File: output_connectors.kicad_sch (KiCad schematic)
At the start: 0 parts

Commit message: feat: add connector footprint and update PCB layout and schematic files
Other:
- added sheet 12V_pwm_fan_output_connector (12V_pwm_fan_output_connector.kicad_sch)
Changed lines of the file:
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@@
 	(generator_version "10.0")
 	(paper "A4")
+	(sheet
+		(at 40.64 36.83)
+		(size 26.67 17.78)
+		(exclude_from_sim no)
+		(in_bom yes)
+		(on_board yes)
+		(dnp no)
+		(fields_autoplaced yes)
+		(stroke
+			(width 0.1524)
+			(type solid)
+		)
+		(fill
+			(color 0 0 0 0)
+		)
+		(property "Sheetname" "12V_pwm_fan_output_connector"
+			(at 40.64 36.1184 0)
+			(show_name no)
+			(do_not_autoplace no)
+			(effects
+				(font
+					(size 1.27 1.27)
+				)
+				(justify left bottom)
+			)
+		)
+		(property "Sheetfile" "12V_pwm_fan_output_connector.kicad_sch"
+			(at 40.64 55.1946 0)
+			(show_name no)
+			(do_not_autoplace no)
+			(effects
+				(font
+					(size 1.27 1.27)
+				)
+				(justify left top)
+			)
+		)
+		(pin "shared_pwm_signal" input
+			(at 40.64 45.72 180)
+			(effects
+				(font
+					(size 1.27 1.27)
+				)
+				(justify left)
+			)
+		)
+		(instances
+			(project "12V_pwm_pump_and_fan_adaptor_board"
+				(path "/1e5bcf57-ecaf-4c00-86fd-4242d519fbb4/c95f4ce9-2da9-4d9d-82ce-79bb5b8b04da"
+					(page "5")
+				)
+			)
+		)
+	)
 )

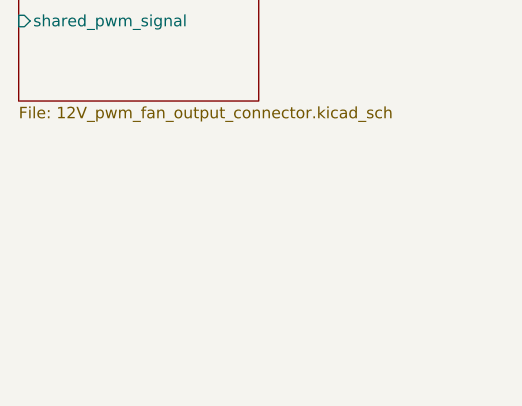
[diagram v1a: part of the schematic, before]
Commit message: feat: add 3D model for 350424-1 connector to library
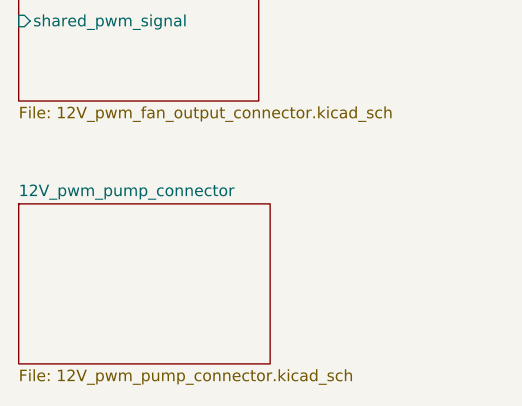
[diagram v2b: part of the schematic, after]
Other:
- added sheet 12V_pwm_pump_connector (12V_pwm_pump_connector.kicad_sch)
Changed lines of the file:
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@@
 	(paper "A4")
+	(sheet
+		(at 40.64 66.04)
+		(size 27.94 17.78)
+		(exclude_from_sim no)
+		(in_bom yes)
+		(on_board yes)
+		(dnp no)
+		(fields_autoplaced yes)
+		(stroke
+			(width 0.1524)
+			(type solid)
+		)
+		(fill
+			(color 0 0 0 0)
+		)
+		(property "Sheetname" "12V_pwm_pump_connector"
+			(at 40.64 65.3284 0)
+			(show_name no)
+			(do_not_autoplace no)
+			(effects
+				(font
+					(size 1.27 1.27)
+				)
+				(justify left bottom)
+			)
+		)
+		(property "Sheetfile" "12V_pwm_pump_connector.kicad_sch"
+			(at 40.64 84.4046 0)
+			(show_name no)
+			(do_not_autoplace no)
+			(effects
+				(font
+					(size 1.27 1.27)
+				)
+				(justify left top)
+			)
+		)
+		(instances
+			(project "12V_pwm_pump_and_fan_adaptor_board"
+				(path "/1e5bcf57-ecaf-4c00-86fd-4242d519fbb4/c95f4ce9-2da9-4d9d-82ce-79bb5b8b04da"
+					(page "6")
+				)
+			)
+		)
+	)
 	(sheet
 		(at 40.64 36.83)

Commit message: chore: update KiCad project settings and sync internal revision history
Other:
- added sheet 12V_pwm_fan_output_connector1 (12V_pwm_fan_output_connector.kicad_sch)
- added sheet 12V_pwm_fan_output_connector2 (12V_pwm_fan_output_connector.kicad_sch)
- sheet 12V_pwm_pump_connector ports: added shared_pwm_signal; removed none
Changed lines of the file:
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@@
 	(generator_version "10.0")
 	(paper "A4")
+	(wire
+		(pts
+			(xy 38.1 74.93) (xy 40.64 74.93)
+		)
+		(stroke
+			(width 0)
+			(type default)
+		)
+	)
+	(wire
+		(pts
+			(xy 38.1 45.72) (xy 40.64 45.72)
+		)
+		(stroke
+			(width 0)
+			(type default)
+		)
+	)
+	(wire
+		(pts
+			(xy 87.63 45.72) (xy 90.17 45.72)
+		)
+		(stroke
+			(width 0)
+			(type default)
+		)
+	)
+	(wire
+		(pts
+			(xy 140.97 45.72) (xy 143.51 45.72)
+		)
+		(stroke
+			(width 0)
+			(type default)
+		)
+	)
+	(hierarchical_label "shared_pwm_signal"
+		(shape input)
+		(at 87.63 45.72 180)
+		(effects
+			(font
+				(size 1.27 1.27)
+			)
+			(justify right)
+		)
+	)
+	(hierarchical_label "shared_pwm_signal"
+		(shape input)
+		(at 38.1 74.93 180)
+		(effects
+			(font
+				(size 1.27 1.27)
+			)
+			(justify right)
+		)
+	)
+	(hierarchical_label "shared_pwm_signal"
+		(shape input)
+		(at 140.97 45.72 180)
+		(effects
+			(font
+				(size 1.27 1.27)
+			)
+			(justify right)
+		)
+	)
+	(hierarchical_label "shared_pwm_signal"
+		(shape input)
+		(at 38.1 45.72 180)
+		(effects
+			(font
+				(size 1.27 1.27)
+			)
+			(justify right)
+		)
+	)
 	(sheet
 		(at 40.64 66.04)
@@
 			)
 		)
+		(pin "shared_pwm_signal" input
+			(at 40.64 74.93 180)
+			(effects
+				(font
+					(size 1.27 1.27)
+				)
+				(justify left)
+			)
+		)
 		(instances
 			(project "12V_pwm_pump_and_fan_adaptor_board"
@@
 				)
 			)
+		)
+	)
+	(sheet
+		(at 90.17 36.83)
+		(size 26.67 17.78)
+		(exclude_from_sim no)
+		(in_bom yes)
+		(on_board yes)
+		(dnp no)
+		(fields_autoplaced yes)
+		(stroke
+			(width 0.1524)
+			(type solid)
+		)
+		(fill
+			(color 0 0 0 0)
+		)
+		(property "Sheetname" "12V_pwm_fan_output_connector1"
+			(at 90.17 36.1184 0)
+			(show_name no)
+			(do_not_autoplace no)
+			(effects
+				(font
+					(size 1.27 1.27)
+				)
+				(justify left bottom)
+			)
+		)
+		(property "Sheetfile" "12V_pwm_fan_output_connector.kicad_sch"
+			(at 90.17 55.1946 0)
+			(show_name no)
+			(do_not_autoplace no)
+			(effects
+				(font
+					(size 1.27 1.27)
+				)
+				(justify left top)
+			)
+		)
+		(pin "shared_pwm_signal" input
+			(at 90.17 45.72 180)
+			(effects
+				(font
+					(size 1.27 1.27)
+				)
+				(justify left)
+			)
+		)
+		(instances
+			(project "12V_pwm_pump_and_fan_adaptor_board"
+				(path "/1e5bcf57-ecaf-4c00-86fd-4242d519fbb4/c95f4ce9-2da9-4d9d-82ce-79bb5b8b04da"
+					(page "7")
+				)
+			)
+		)
+	)
+	(sheet
+		(at 143.51 36.83)
+		(size 26.67 17.78)
+		(exclude_from_sim no)
+		(in_bom yes)
+		(on_board yes)
+		(dnp no)
+		(fields_autoplaced yes)
+		(stroke
+			(width 0.1524)
+			(type solid)
+		)
+		(fill
+			(color 0 0 0 0)
+		)
+		(property "Sheetname" "12V_pwm_fan_output_connector2"
+			(at 143.51 36.1184 0)
+			(show_name no)
+			(do_not_autoplace no)
+			(effects
+				(font
+					(size 1.27 1.27)
+				)
+				(justify left bottom)
+			)
+		)
+		(property "Sheetfile" "12V_pwm_fan_output_connector.kicad_sch"
+			(at 143.51 55.1946 0)
+			(show_name no)
+			(do_not_autoplace no)
+			(effects
+				(font
+					(size 1.27 1.27)
+				)
+				(justify left top)
+			)
+		)
+		(pin "shared_pwm_signal" input
+			(at 143.51 45.72 180)
+			(effects
+				(font
+					(size 1.27 1.27)
+				)
+				(justify left)
+			)
+		)
+		(instances
+			(project "12V_pwm_pump_and_fan_adaptor_board"
+				(path "/1e5bcf57-ecaf-4c00-86fd-4242d519fbb4/c95f4ce9-2da9-4d9d-82ce-79bb5b8b04da"
+					(page "8")
+				)
+			)
